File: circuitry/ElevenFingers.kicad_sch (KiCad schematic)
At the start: 35 parts

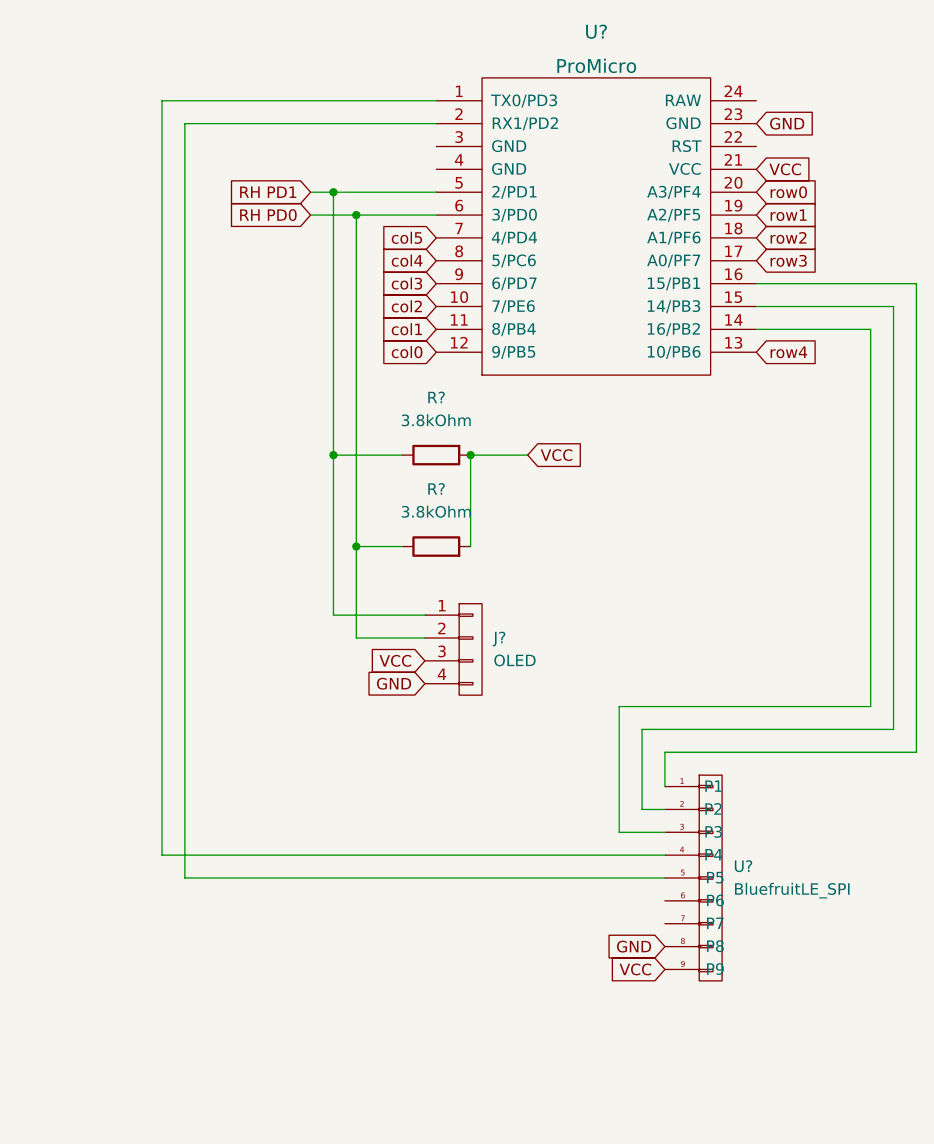
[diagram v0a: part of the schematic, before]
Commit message: moved row0-4 and col0-5 pins
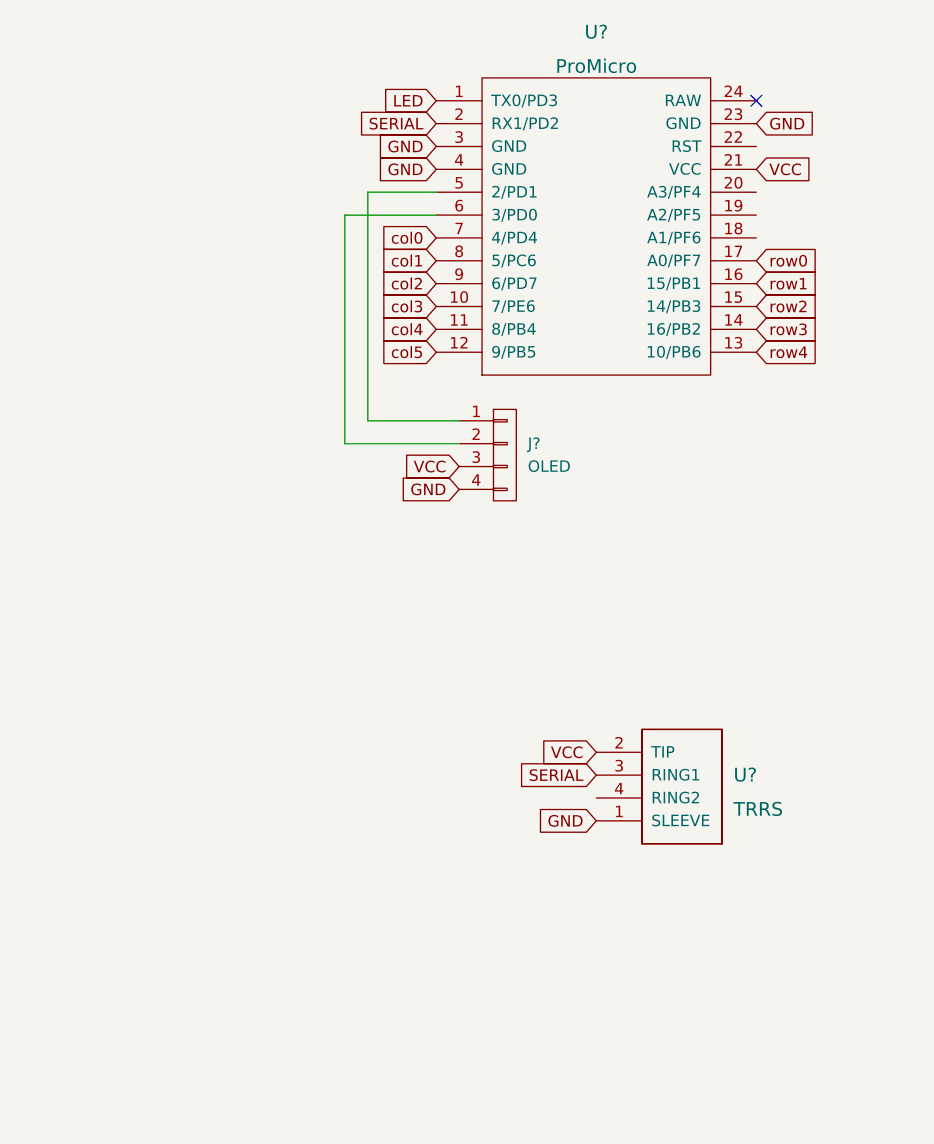
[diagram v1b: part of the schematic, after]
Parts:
- removed R? (x2): 3.8kOhm, symbol Device:R
- removed U?: BluefruitLE_SPI, symbol ElevenFingers:BluefruitLE_SPI
- added U?: TRRS, symbol keebio:TRRS
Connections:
- net GND: now also U?.3 (GND), U?.4 (GND), U?.1 (SLEEVE)
- net VCC: now also U?.2 (TIP)
- net col0: now also U?.7 (4/PD4); no longer U?.12 (9/PB5)
- net col1: now also U?.8 (5/PC6); no longer U?.11 (8/PB4)
- net col2: now also U?.9 (6/PD7); no longer U?.10 (7/PE6)
- net col3: now also U?.10 (7/PE6); no longer U?.9 (6/PD7)
- net col4: now also U?.11 (8/PB4); no longer U?.8 (5/PC6)
- net col5: now also U?.12 (9/PB5); no longer U?.7 (4/PD4)
- net row0: now also U?.17 (A0/PF7); no longer U?.20 (A3/PF4)
- net row1: now also U?.16 (15/PB1); no longer U?.19 (A2/PF5)
- net row2: now also U?.15 (14/PB3); no longer U?.18 (A1/PF6)
- net row3: now also U?.14 (16/PB2); no longer U?.17 (A0/PF7)
- net LED: now reaches U?.1 (TX0/PD3)
- net SERIAL: now reaches U?.2 (RX1/PD2)
- net SERIAL: now also U?.3 (RING1)
- net RH PD0: no longer names the net of J?.2 (P2), U?.6 (3/PD0)
- net RH PD1: no longer names the net of J?.1 (P1), U?.5 (2/PD1)
- no-connect marks 0 -> 1
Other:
- moved on the sheet: J?

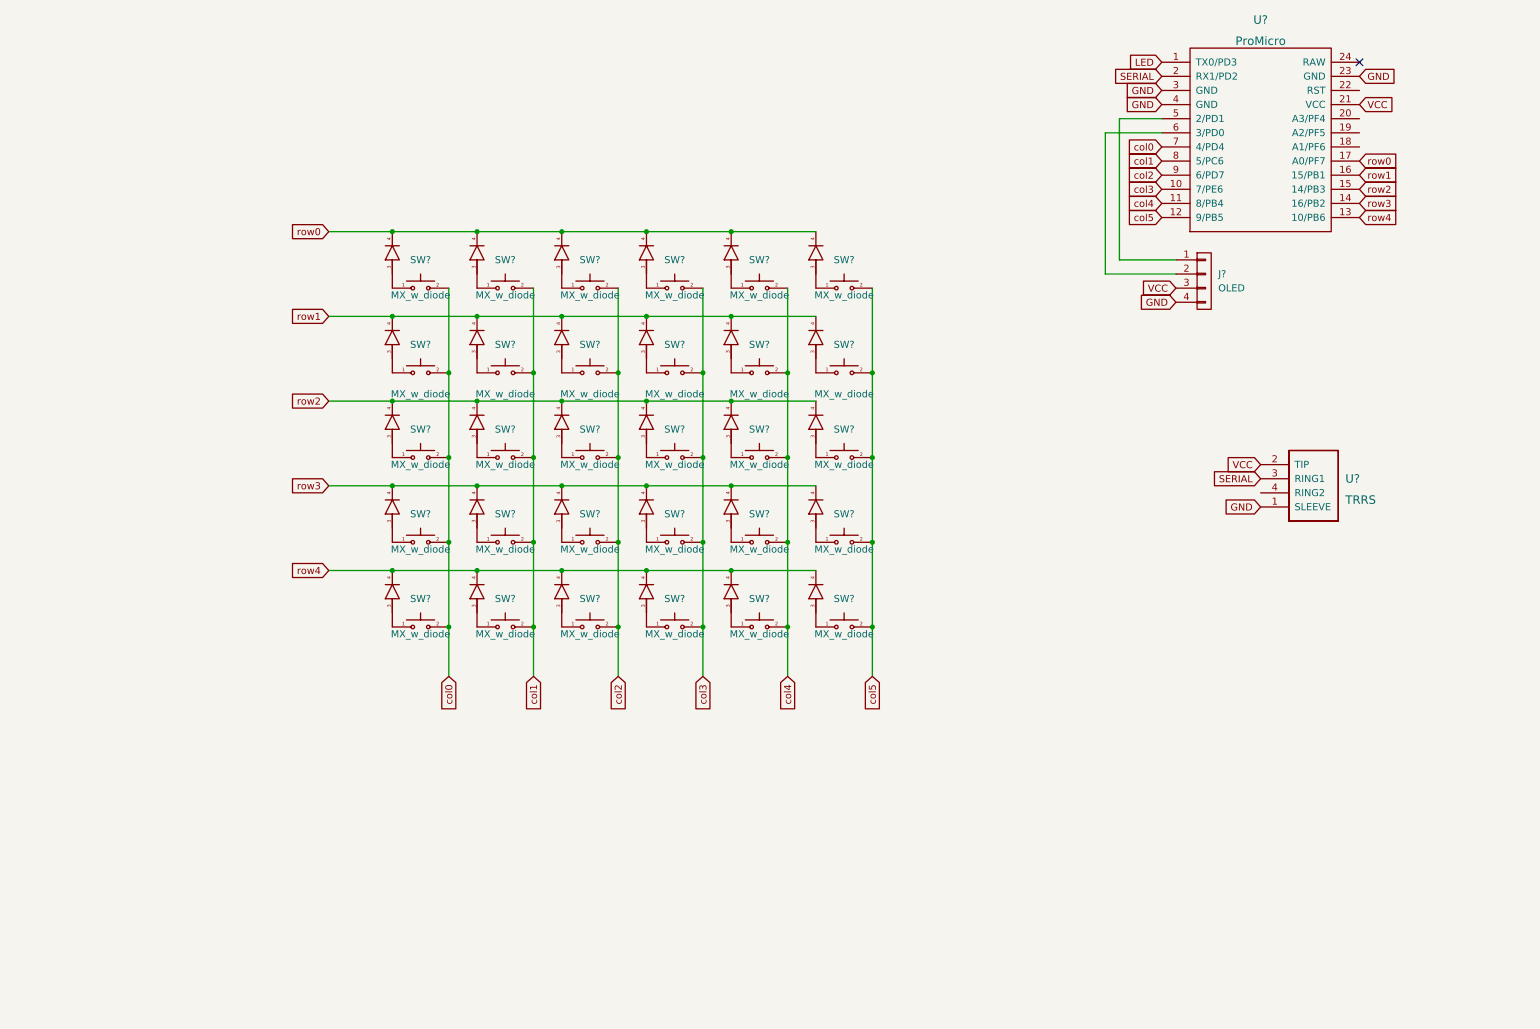
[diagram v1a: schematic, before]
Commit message: finished schematic, customized footprints, organized pcb
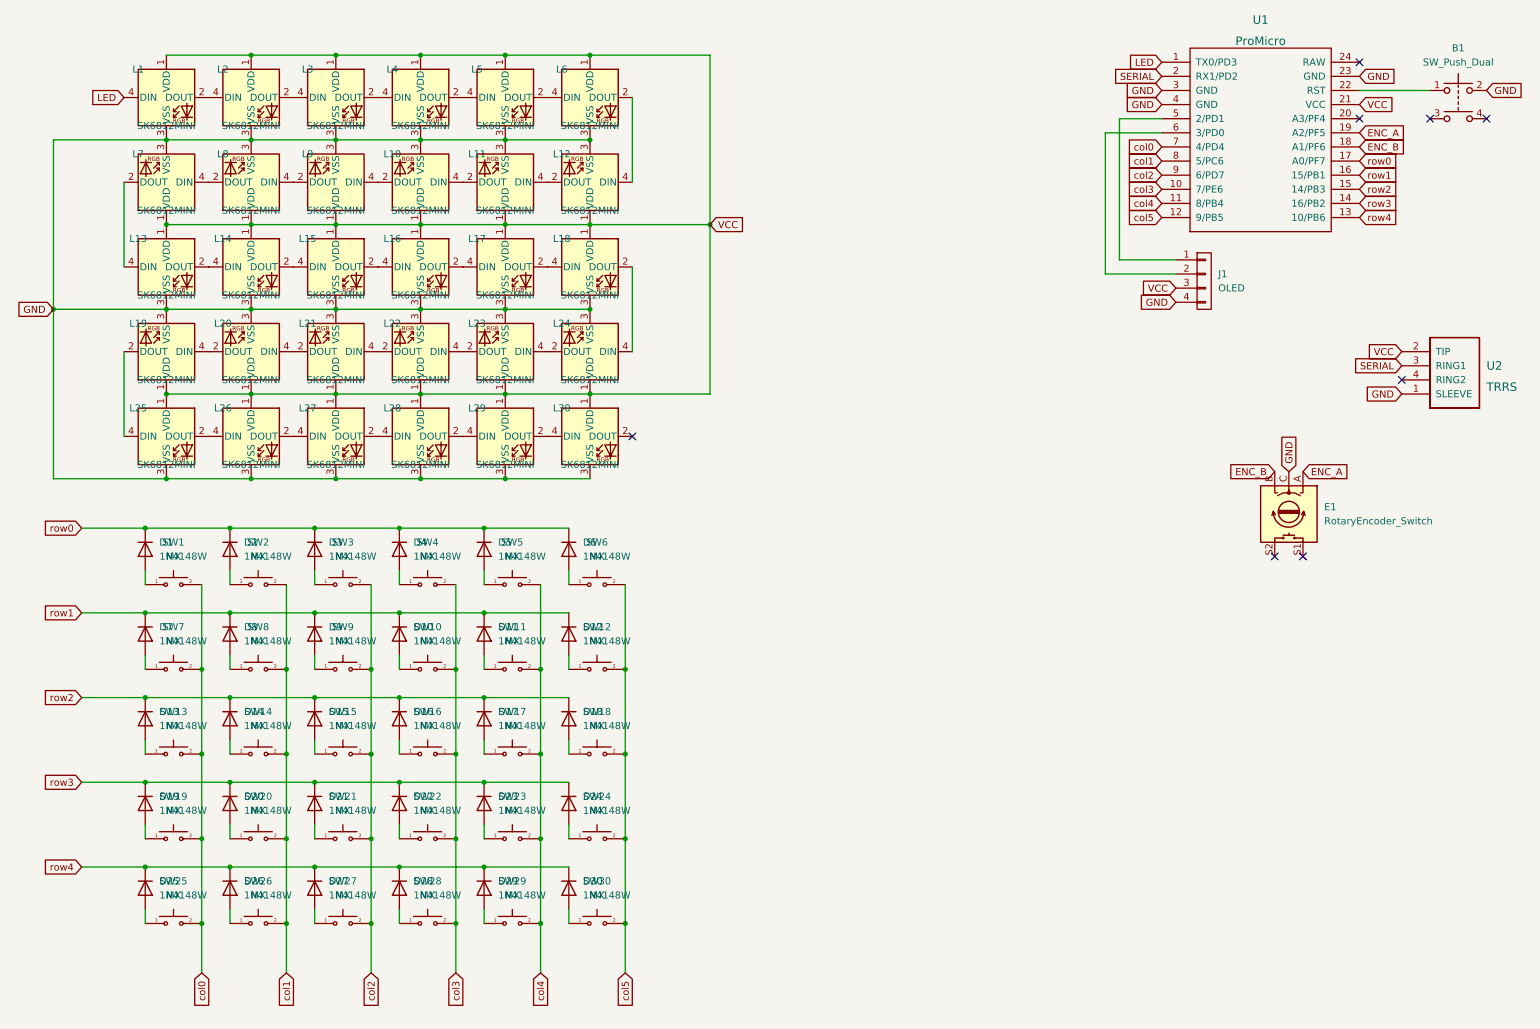
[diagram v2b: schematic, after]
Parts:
- removed SW? (x30): MX_w_diode, symbol ElevenFingers:MX_w_diode
- added B1: SW_Push_Dual, ElevenFingers:Arduino_Pushbutton, symbol Switch:SW_Push_Dual
- added D1, D10, D11, D12, D13, D14, D15, D16, D17, D18, D19, D2, D20, D21, D22, D23, D24, D25, D26, D27, D28, D29, D3, D30, D4, D5, D6, D7, D8, D9: 1N4148W, ElevenFingers:D_SOD-123, symbol Diode:1N4148W
- added E1: RotaryEncoder_Switch, ElevenFingers:RotaryEncoder_EC11, symbol Device:RotaryEncoder_Switch
- added L1, L10, L11, L12, L13, L14, L15, L16, L17, L18, L19, L2, L20, L21, L22, L23, L24, L25, L26, L27, L28, L29, L3, L30, L4, L5, L6, L7, L8, L9: SK6812MINI, ElevenFingers:LED_SK6812MINI_PLCC4_3.5x3.5mm_P1.75mm, symbol ElevenFingers:SK6812MINI
- added SW1, SW10, SW11, SW12, SW13, SW14, SW15, SW16, SW17, SW18, SW19, SW2, SW20, SW21, SW22, SW23, SW24, SW25, SW26, SW27, SW28, SW29, SW3, SW30, SW4, SW5, SW6, SW7, SW8, SW9: MX, ElevenFingers:SW_Cherry_MX_1.00u_PCB, symbol ElevenFingers:MX
- J1: renamed from J?; footprint (none) -> ElevenFingers:OLED_4Pin
- U1: renamed from U?; footprint (none) -> ElevenFingers:ProMicro
- U2: renamed from U?; footprint (none) -> ElevenFingers:TRRS-PJ-320A
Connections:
- net GND: now also B1.2, E1.C, L1.3 (VSS), L10.3 (VSS), L11.3 (VSS), L12.3 (VSS), L13.3 (VSS), L14.3 (VSS), L15.3 (VSS), L16.3 (VSS), L17.3 (VSS), L18.3 (VSS), L19.3 (VSS), L2.3 (VSS), L20.3 (VSS), L21.3 (VSS), L22.3 (VSS), L23.3 (VSS), L24.3 (VSS), L25.3 (VSS), L26.3 (VSS), L27.3 (VSS), L28.3 (VSS), L29.3 (VSS), L3.3 (VSS), L30.3 (VSS), L4.3 (VSS), L5.3 (VSS), L6.3 (VSS), L7.3 (VSS), L8.3 (VSS), L9.3 (VSS)
- net LED: now also L1.4 (DIN)
- net VCC: now also L1.1 (VDD), L10.1 (VDD), L11.1 (VDD), L12.1 (VDD), L13.1 (VDD), L14.1 (VDD), L15.1 (VDD), L16.1 (VDD), L17.1 (VDD), L18.1 (VDD), L19.1 (VDD), L2.1 (VDD), L20.1 (VDD), L21.1 (VDD), L22.1 (VDD), L23.1 (VDD), L24.1 (VDD), L25.1 (VDD), L26.1 (VDD), L27.1 (VDD), L28.1 (VDD), L29.1 (VDD), L3.1 (VDD), L30.1 (VDD), L4.1 (VDD), L5.1 (VDD), L6.1 (VDD), L7.1 (VDD), L8.1 (VDD), L9.1 (VDD)
- net col0: now also SW1.2, SW13.2, SW19.2, SW25.2, SW7.2
- net col1: now also SW14.2, SW2.2, SW20.2, SW26.2, SW8.2
- net col2: now also SW15.2, SW21.2, SW27.2, SW3.2, SW9.2
- net col3: now also SW10.2, SW16.2, SW22.2, SW28.2, SW4.2
- net col4: now also SW11.2, SW17.2, SW23.2, SW29.2, SW5.2
- net col5: now also SW12.2, SW18.2, SW24.2, SW30.2, SW6.2
- net row0: now also D1.1 (K), D2.1 (K), D3.1 (K), D4.1 (K), D5.1 (K), D6.1 (K)
- net row1: now also D10.1 (K), D11.1 (K), D12.1 (K), D7.1 (K), D8.1 (K), D9.1 (K)
- net row2: now also D13.1 (K), D14.1 (K), D15.1 (K), D16.1 (K), D17.1 (K), D18.1 (K)
- net row3: now also D19.1 (K), D20.1 (K), D21.1 (K), D22.1 (K), D23.1 (K), D24.1 (K)
- net row4: now also D25.1 (K), D26.1 (K), D27.1 (K), D28.1 (K), D29.1 (K), D30.1 (K)
- net ENC_B: now reaches U1.18 (A1/PF6)
- net ENC_B: now also E1.B
- net ENC_A: now reaches U1.19 (A2/PF5)
- net ENC_A: now also E1.A
- net at U1.22 (RST): now also B1.1
- new net: L17.2 (DOUT), L18.4 (DIN)
- new net: L16.2 (DOUT), L17.4 (DIN)
- new net: L4.2 (DOUT), L5.4 (DIN)
- new net: L3.2 (DOUT), L4.4 (DIN)
- new net: L18.2 (DOUT), L24.4 (DIN)
- new net: L2.2 (DOUT), L3.4 (DIN)
- new net: L1.2 (DOUT), L2.4 (DIN)
- new net: D15.2 (A), SW15.1
- new net: D12.2 (A), SW12.1
- new net: L22.4 (DIN), L23.2 (DOUT)
- new net: L23.4 (DIN), L24.2 (DOUT)
- new net: D29.2 (A), SW29.1
- new net: L20.4 (DIN), L21.2 (DOUT)
- new net: L21.4 (DIN), L22.2 (DOUT)
- new net: D8.2 (A), SW8.1
- new net: D26.2 (A), SW26.1
- new net: D4.2 (A), SW4.1
- new net: D9.2 (A), SW9.1
- new net: L14.2 (DOUT), L15.4 (DIN)
- new net: L13.2 (DOUT), L14.4 (DIN)
- new net: D1.2 (A), SW1.1
- new net: D16.2 (A), SW16.1
- new net: D11.2 (A), SW11.1
- new net: D28.2 (A), SW28.1
- new net: L26.2 (DOUT), L27.4 (DIN)
- new net: L25.2 (DOUT), L26.4 (DIN)
- new net: D21.2 (A), SW21.1
- new net: D5.2 (A), SW5.1
- new net: D30.2 (A), SW30.1
- new net: D24.2 (A), SW24.1
- new net: D19.2 (A), SW19.1
- new net: D10.2 (A), SW10.1
- new net: D17.2 (A), SW17.1
- new net: D7.2 (A), SW7.1
- new net: D6.2 (A), SW6.1
- new net: D27.2 (A), SW27.1
- new net: L29.2 (DOUT), L30.4 (DIN)
- new net: L28.2 (DOUT), L29.4 (DIN)
- new net: D14.2 (A), SW14.1
- new net: D23.2 (A), SW23.1
- new net: L15.2 (DOUT), L16.4 (DIN)
- new net: D20.2 (A), SW20.1
- new net: L10.2 (DOUT), L9.4 (DIN)
- new net: L10.4 (DIN), L11.2 (DOUT)
- new net: L11.4 (DIN), L12.2 (DOUT)
- new net: L12.4 (DIN), L6.2 (DOUT)
- new net: L27.2 (DOUT), L28.4 (DIN)
- new net: L8.4 (DIN), L9.2 (DOUT)
- new net: D3.2 (A), SW3.1
- new net: L19.4 (DIN), L20.2 (DOUT)
- new net: L19.2 (DOUT), L25.4 (DIN)
- new net: L13.4 (DIN), L7.2 (DOUT)
- new net: L7.4 (DIN), L8.2 (DOUT)
- new net: D25.2 (A), SW25.1
- new net: L5.2 (DOUT), L6.4 (DIN)
- new net: D13.2 (A), SW13.1
- new net: D18.2 (A), SW18.1
- new net: D22.2 (A), SW22.1
- new net: D2.2 (A), SW2.1
- no-connect marks 1 -> 8
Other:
- moved on the sheet: U2
